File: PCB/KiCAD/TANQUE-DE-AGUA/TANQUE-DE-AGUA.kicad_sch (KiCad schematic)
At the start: 43 parts, among them J2 Vca_OUT, J3 DC IN, J5 HX30002-BA, Q1 2N3904, SW1 Nivel MAX, SW2 Nivel Min, U1 74HC00, U2 ULN2003, U3 LM7805, U4 74HC14, U5 MOC3021M, U6 BTA16-600C

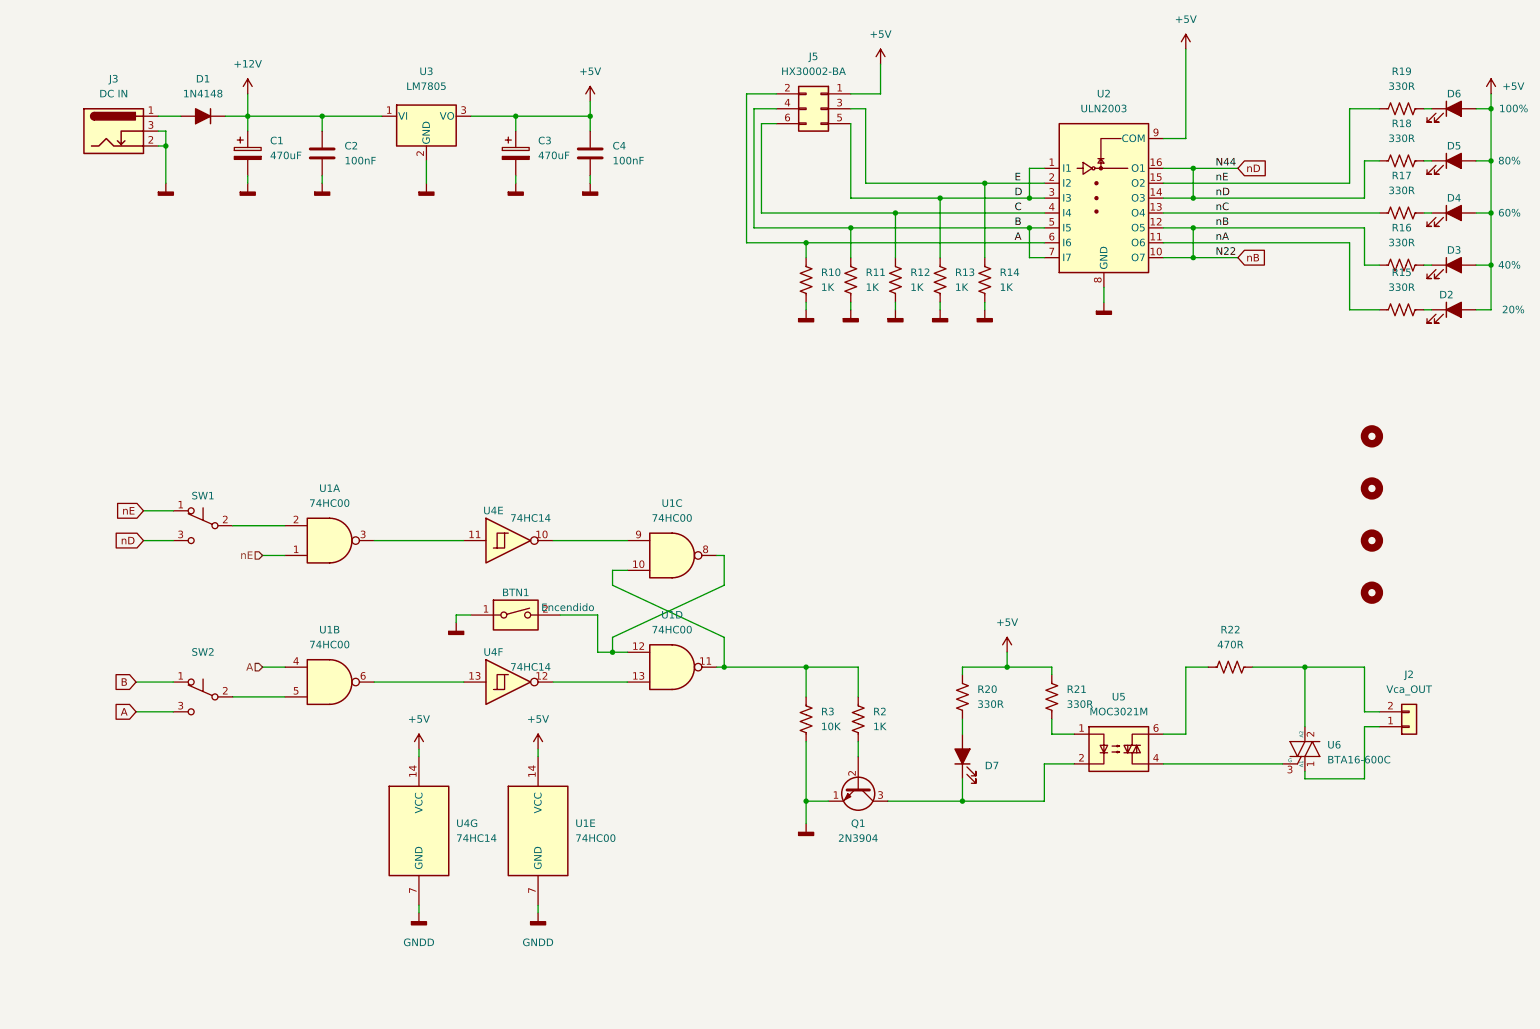
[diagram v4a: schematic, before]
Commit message: se agrega Fuente capacitiva
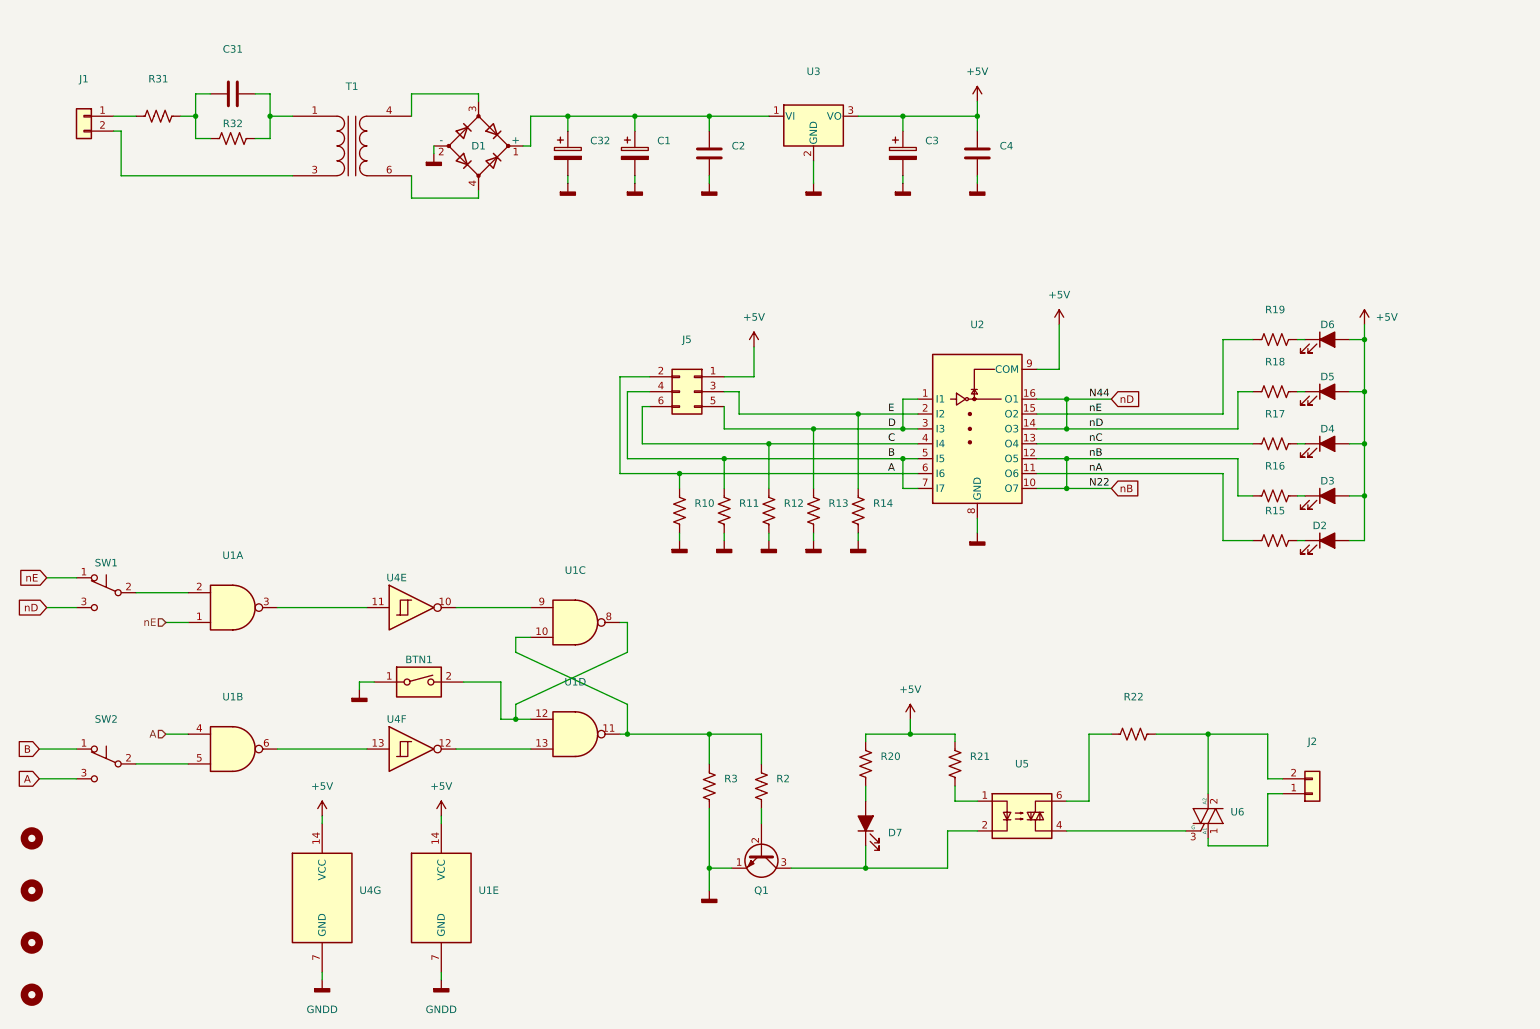
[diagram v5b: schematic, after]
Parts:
- removed D1: 1N4148, Diode_THT:D_A-405_P7.62mm_Horizontal, symbol Device:D_Filled
- removed J3: DC IN, Connector_BarrelJack:BarrelJack_Horizontal, symbol Connector:Barrel_Jack_Switch
- added C31: (no value), symbol Device:C
- added C32: (no value), symbol Device:C_Polarized
- added D1: (no value), symbol Device:D_Bridge_+-AA
- added J1: (no value), symbol Connector_Generic:Conn_01x02
- added R31, R32: (no value), symbol Device:R_US
- added T1: (no value), symbol Device:Transformer_1P_1S
- BTN1: value Encendido -> (none); footprint Button_Switch_THT:SW_PUSH_6mm_H4.3mm -> (none)
- C1, C3: value 470uF -> (none)
- C2, C4: value 100nF -> (none); footprint Capacitor_THT:C_Disc_D7.5mm_W2.5mm_P5.00mm -> (none)
- D2: value 20% -> (none); footprint LED_THT:LED_D3.0mm -> (none)
- D3: value 40% -> (none); footprint LED_THT:LED_D3.0mm -> (none)
- D4: value 60% -> (none); footprint LED_THT:LED_D3.0mm -> (none)
- D5: value 80% -> (none); footprint LED_THT:LED_D3.0mm -> (none)
- D6: value 100% -> (none); footprint LED_THT:LED_D3.0mm -> (none)
- D7: value ENCENDIDO -> (none); footprint LED_THT:LED_D3.0mm_IRGrey -> (none)
- H1, H2, H3, H4: value MountingHole -> (none); footprint MountingHole:MountingHole_2.7mm_M2.5 -> (none)
- J2: value Vca_OUT -> (none); footprint TerminalBlock_Phoenix:TerminalBlock_Phoenix_MPT-0,5-2-2.54_1x02_P2.54mm_Horizontal -> (none)
- J5: value HX30002-BA -> (none); footprint Connector_PinSocket_2.54mm:PinSocket_2x03_P2.54mm_Vertical -> (none)
- Q1: value 2N3904 -> (none); footprint Package_TO_SOT_THT:TO-92_Wide -> (none)
- R10, R11, R12, R13, R14, R2: value 1K -> (none); footprint Resistor_THT:R_Axial_DIN0207_L6.3mm_D2.5mm_P10.16mm_Horizontal -> (none)
- R15, R16, R17, R18, R19, R20, R21: value 330R -> (none); footprint Resistor_THT:R_Axial_DIN0207_L6.3mm_D2.5mm_P10.16mm_Horizontal -> (none)
- R22: value 470R -> (none); footprint Resistor_THT:R_Axial_DIN0207_L6.3mm_D2.5mm_P10.16mm_Horizontal -> (none)
- R3: value 10K -> (none); footprint Resistor_THT:R_Axial_DIN0207_L6.3mm_D2.5mm_P10.16mm_Horizontal -> (none)
- SW1: value Nivel MAX -> (none); footprint Connector_PinHeader_2.54mm:PinHeader_1x03_P2.54mm_Vertical -> (none)
- SW2: value Nivel Min -> (none); footprint Connector_PinHeader_2.54mm:PinHeader_1x03_P2.54mm_Vertical -> (none)
- U1: value 74HC00 -> (none); footprint Package_DIP:DIP-14_W7.62mm_LongPads -> (none)
- U2: value ULN2003 -> (none); footprint Package_DIP:DIP-16_W7.62mm_LongPads -> (none)
- U3: value LM7805 -> (none); footprint Package_TO_SOT_THT:TO-220-3_Vertical -> (none)
- U4: value 74HC14 -> (none); footprint Package_DIP:DIP-14_W7.62mm_LongPads -> (none)
- U5: value MOC3021M -> (none); footprint Package_DIP:DIP-6_W7.62mm_LongPads -> (none)
- U6: value BTA16-600C -> (none); footprint Package_TO_SOT_THT:TO-220-3_Vertical -> (none)
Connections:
- net GNDD: now also C32.2, D1.2 (-)
- net nA: now also R15.1; no longer R15.2
- net nB: now also R16.1; no longer R16.2
- net nC: now also R17.1; no longer R17.2
- net nD: now also R18.1; no longer R18.2
- net nE: now also R19.1; no longer R19.2
- net at D2.1 (K): now also R15.2; no longer R15.1
- net at D3.1 (K): now also R16.2; no longer R16.1
- net at D4.1 (K): now also R17.2; no longer R17.1
- net at D5.1 (K): now also R18.2; no longer R18.1
- net at D6.1 (K): now also R19.2; no longer R19.1
- net +12V: no longer names the net of C1.1, C2.1, U3.1 (VI)
- net +12V: now also C32.1, D1.1 (+)
- new net: C31.1, R31.2, R32.1
- new net: C31.2, R32.2, T1.1 (AA)
- new net: J1.1 (Pin_1), R31.1
- new net: J1.2 (Pin_2), T1.3 (AB)
- new net: D1.3, T1.4 (SB)
- new net: D1.4, T1.6 (SA)
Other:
- moved on the sheet: BTN1, C1, C2, C3, C4, D2, D3, D4, D5, D6, D7, J2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

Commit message: update PCB
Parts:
- BTN1: value (none) -> Encendido; footprint (none) -> Button_Switch_THT:SW_PUSH_6mm_H4.3mm
- C1, C3: value (none) -> 470uF; footprint (none) -> Capacitor_THT:CP_Radial_D8.0mm_P3.50mm
- C2, C4: value (none) -> 100nF; footprint (none) -> Capacitor_THT:C_Disc_D7.5mm_W2.5mm_P5.00mm
- C31: value (none) -> 1000nF; footprint (none) -> Capacitor_THT:C_Rect_L9.0mm_W4.0mm_P7.50mm_MKT
- C32: value (none) -> 100uF; footprint (none) -> Capacitor_THT:CP_Radial_D8.0mm_P3.50mm
- D1: value (none) -> D_Bridge_+-AA; footprint (none) -> Diode_THT:Diode_Bridge_19.0x3.5x10.0mm_P5.0mm
- D2: value (none) -> 20%; footprint (none) -> LED_THT:LED_D3.0mm
- D3: value (none) -> 40%; footprint (none) -> LED_THT:LED_D3.0mm
- D4: value (none) -> 60%; footprint (none) -> LED_THT:LED_D3.0mm
- D5: value (none) -> 80%; footprint (none) -> LED_THT:LED_D3.0mm
- D6: value (none) -> 100%; footprint (none) -> LED_THT:LED_D3.0mm
- D7: value (none) -> ENCENDIDO; footprint (none) -> LED_THT:LED_D3.0mm_IRGrey
- H1, H2, H3, H4: value (none) -> MountingHole; footprint (none) -> MountingHole:MountingHole_4.3mm_M4
- J1: value (none) -> Vca_IN; footprint (none) -> TerminalBlock_Phoenix:TerminalBlock_Phoenix_PT-1,5-2-5.0-H_1x02_P5.00mm_Horizontal
- J2: value (none) -> Vca_OUT; footprint (none) -> TerminalBlock_Phoenix:TerminalBlock_Phoenix_PT-1,5-2-5.0-H_1x02_P5.00mm_Horizontal
- J5: value (none) -> HX30002-BA; footprint (none) -> Connector_PinSocket_2.54mm:PinSocket_2x03_P2.54mm_Vertical
- Q1: value (none) -> 2N3904; footprint (none) -> Package_TO_SOT_THT:TO-92_Wide
- R10, R11, R12, R13, R14, R2: value (none) -> 1K; footprint (none) -> Resistor_THT:R_Axial_DIN0207_L6.3mm_D2.5mm_P10.16mm_Horizontal
- R15, R16, R17, R18, R19: value (none) -> 330R
- R20, R21: value (none) -> 330R; footprint (none) -> Resistor_THT:R_Axial_DIN0207_L6.3mm_D2.5mm_P10.16mm_Horizontal
- R22: value (none) -> 470R; footprint (none) -> Resistor_THT:R_Axial_DIN0207_L6.3mm_D2.5mm_P10.16mm_Horizontal
- R3: value (none) -> 10K; footprint (none) -> Resistor_THT:R_Axial_DIN0207_L6.3mm_D2.5mm_P10.16mm_Horizontal
- R31: value (none) -> 50R; footprint (none) -> Resistor_THT:R_Axial_DIN0207_L6.3mm_D2.5mm_P10.16mm_Horizontal
- R32: value (none) -> 1M; footprint (none) -> Resistor_THT:R_Axial_DIN0207_L6.3mm_D2.5mm_P10.16mm_Horizontal
- SW1: value (none) -> Nivel MAX; footprint (none) -> Connector_PinHeader_2.54mm:PinHeader_1x03_P2.54mm_Vertical
- SW2: value (none) -> Nivel Min; footprint (none) -> Connector_PinHeader_2.54mm:PinHeader_1x03_P2.54mm_Vertical
- T1: value (none) -> Transformer_1P_1S; footprint (none) -> Transformer_THT:Transformer_NF_ETAL_1-1_P1200
- U1: value (none) -> 74HC00; footprint (none) -> Package_DIP:DIP-14_W7.62mm_LongPads
- U2: value (none) -> ULN2003; footprint (none) -> Package_DIP:DIP-16_W7.62mm_LongPads
- U3: value (none) -> LM7805; footprint (none) -> Package_TO_SOT_THT:TO-220-3_Vertical
- U4: value (none) -> 74HC14; footprint (none) -> Package_DIP:DIP-14_W7.62mm_LongPads
- U5: value (none) -> MOC3021M; footprint (none) -> Package_DIP:DIP-6_W7.62mm_LongPads
- U6: value (none) -> BTA16-600C; footprint (none) -> Package_TO_SOT_THT:TO-220-3_Vertical
